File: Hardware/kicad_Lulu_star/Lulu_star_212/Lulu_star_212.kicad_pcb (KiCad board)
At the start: 2 copper layers, 16.7 x 14.9 mm, 6 parts, among them J1 Conn_01x03_Female, Q1 Q_NMOS_GSD, T1 Q_NPN_BEC

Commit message: PCB in progress
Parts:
- LED1: footprint Lulu_footprints:LED_Lulu_side -> Lulu_footprints:Lulu_side_LED
- moved J1 2.90 mm to (123.7, 108.5)
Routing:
- net (no net): vias 0 -> 5
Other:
- board text added: "Lulu V_212"

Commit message: Routing in progress
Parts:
- added J1: Soldering_pad, Lulu_footprints:Lulu_brass_tube_pad, F.Cu at (131.7, 104.8)
- moved R1 0.51 mm to (125.7, 99.8), turned to 180 degrees
- moved Q1 0.25 mm to (128.0, 102.9)
- moved R2 0.15 mm to (130.8, 108.5)
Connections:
- LED1 pad : (no net) -> GND
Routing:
- net Net-(Q1-Pad1): track 0.00 -> 2.27 mm
- net GND: vias 0 -> 4
- net (no net): vias 5 -> 0
- added copper zone on B.Cu, net GND
- added copper zone on F.Cu, net GND
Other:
- board text added: "Lulu"
- board text added: "V-212"
- board text removed: "Lulu V_212"

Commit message: PCB in progress
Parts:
- moved J1 16.0 mm to (139.7, 108.3)
- moved T1 16.0 mm to (140.5, 102.7)
- moved J1 16.0 mm to (147.7, 104.6)
- moved Q1 16.0 mm to (144.0, 102.7)
- moved R2 16.0 mm to (146.8, 108.3)
- moved R1 16.0 mm to (141.7, 99.6)
- moved LED1 16.0 mm to (146.4, 99.9)
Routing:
- net Net-(Q1-Pad2): track 0.00 -> 9.05 mm, vias 0 -> 2
- net Net-(Q1-Pad1): track 2.27 -> 6.60 mm
- net +3V3: track 0.00 -> 1.27 mm
- net Net-(LED1-Pad1): track 0.00 -> 0.65 mm
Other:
- outline, holes or cut-outs redrawn

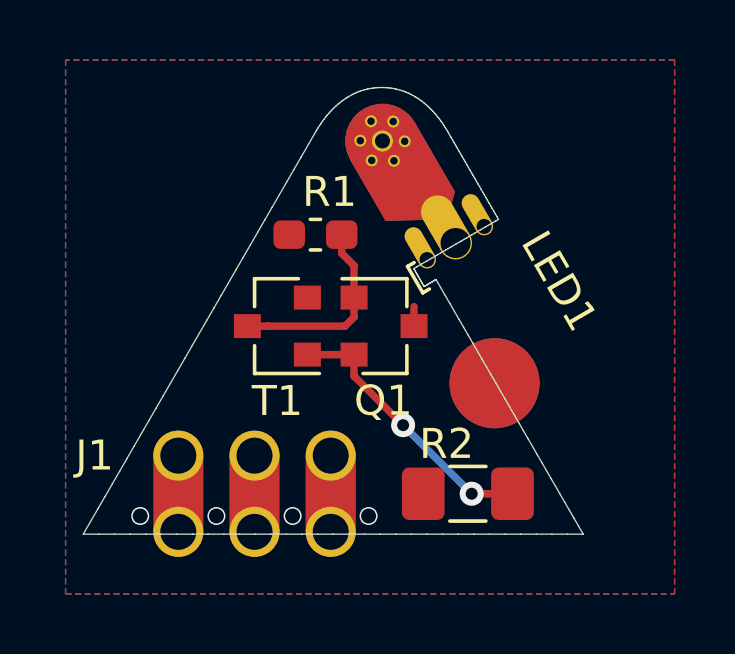
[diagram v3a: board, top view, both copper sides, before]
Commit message: Added PCB pin fonctions top & bottom
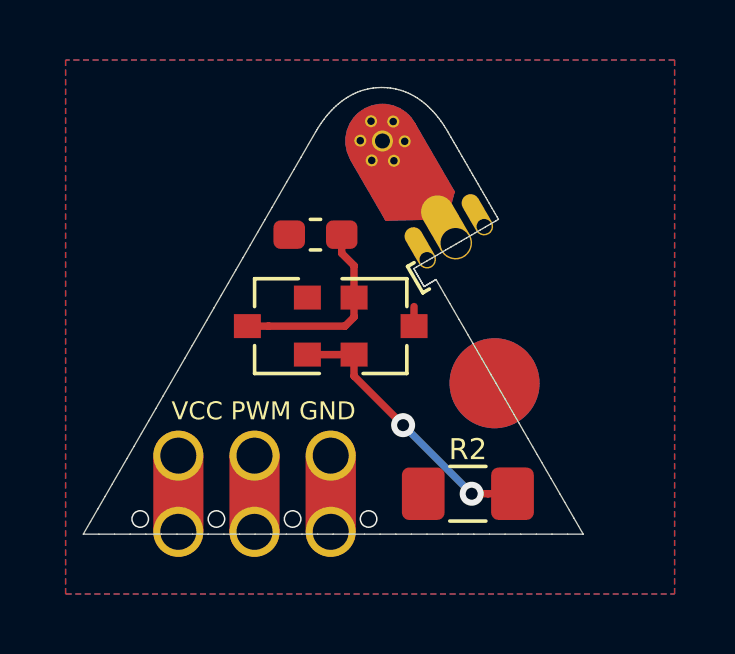
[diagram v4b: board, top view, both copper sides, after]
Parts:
- R1: value 47 K -> 47K
- R2: value 2.7 Ohm -> 2.7-Ohm
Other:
- board text added: "GND PWM VCC"
- board text added: "V.212"
- board text added: "VCC PWM GND"
- board text removed: "V-212"
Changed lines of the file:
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@@
   (general
     (thickness 1)
-    (drawings 290)
+    (drawings 292)
     (tracks 21)
     (zones 0)
@@
     (44 Edge.Cuts user)
     (45 Margin user)
-    (46 B.CrtYd user hide)
-    (47 F.CrtYd user hide)
+    (46 B.CrtYd user)
+    (47 F.CrtYd user)
     (48 B.Fab user)
-    (49 F.Fab user hide)
+    (49 F.Fab user)
   )
   (setup
@@
     (mod_text_size 1 1)
     (mod_text_width 0.15)
-    (pad_size 1.425 1.75)
+    (pad_size 1.675 4.2)
     (pad_drill 0)
     (pad_to_mask_clearance 0)
@@
     (tags "LED Cree XP")
     (attr smd)
-    (fp_text reference LED1 (at 2.35166 2.831161 120.1) (layer F.SilkS)
-      (effects (font (size 1 1) (thickness 0.15)))
-    )
-    (fp_text value LED_PAD (at 2.400901 -2.571716 300.1) (layer F.Fab)
+    (fp_text reference LED1 (at 2.35166 2.831161 120.1) (layer F.SilkS) hide
+      (effects (font (size 1 1) (thickness 0.15)))
+    )
+    (fp_text value LED_PAD (at 2.400901 -2.571716 -59.9) (layer F.Fab) hide
       (effects (font (size 1 1) (thickness 0.15)))
     )
@@
     (pad 3 thru_hole circle (at -1.037581 -4.544671 120.1) (size 0.4 0.4) (drill 0.25) (layers *.Cu)
       (net 2 GND))
-    (pad 3 thru_hole circle (at -0.402581 -4.925671 120.1) (size 0.4 0.4) (drill 0.25) (layers *.Cu)
+    (pad 3 thru_hole circle (at -0.40258 -4.925671 120.1) (size 0.4 0.4) (drill 0.25) (layers *.Cu)
       (net 2 GND))
     (pad 3 thru_hole circle (at -0.402581 -4.163672 120.1) (size 0.7 0.7) (drill 0.5) (layers *.Cu)
@@
     (tags eTextile)
     (zone_connect 0)
-    (fp_text reference J1 (at -5.334 -1.27) (layer F.SilkS)
-      (effects (font (size 1 1) (thickness 0.15)))
-    )
-    (fp_text value Conn_01x03_Female (at 0 3.175) (layer F.Fab)
+    (fp_text reference J1 (at -5.334 -1.27) (layer F.SilkS) hide
+      (effects (font (size 1 1) (thickness 0.15)))
+    )
+    (fp_text value Conn_01x03_Female (at 0 3.175) (layer F.Fab) hide
       (effects (font (size 1 1) (thickness 0.15)))
     )
@@
       (effects (font (size 1 1) (thickness 0.15)))
     )
-    (fp_text value Soldering_pad (at -1.018116 -4.840572 120) (layer F.Fab)
+    (fp_text value Soldering_pad (at -1.018116 -4.840572 120) (layer F.Fab) hide
       (effects (font (size 1 1) (thickness 0.15)))
     )
@@
     (tags SOT-23)
     (attr smd)
-    (fp_text reference T1 (at 0 -2.5 180) (layer F.SilkS)
-      (effects (font (size 1 1) (thickness 0.15)))
-    )
-    (fp_text value Q_NPN_BEC (at 0 2.5 180) (layer F.Fab)
+    (fp_text reference T1 (at 0 -2.5 180) (layer F.SilkS) hide
+      (effects (font (size 1 1) (thickness 0.15)))
+    )
+    (fp_text value Q_NPN_BEC (at 0 2.5 180) (layer F.Fab) hide
       (effects (font (size 1 1) (thickness 0.15)))
     )
@@
       (net 3 "Net-(Q1-Pad1)"))
     (pad 2 smd rect (at -1 0.95 180) (size 0.9 0.8) (layers F.Cu F.Paste F.Mask)
-      (net 2 GND))
+      (net 2 GND) (zone_connect 1))
     (pad 1 smd rect (at -1 -0.95 180) (size 0.9 0.8) (layers F.Cu F.Paste F.Mask)
       (net 1 "Net-(Q1-Pad2)"))
@@
     (tags SOT-23)
     (attr smd)
-    (fp_text reference Q1 (at -0.0254 2.4892) (layer F.SilkS)
-      (effects (font (size 1 1) (thickness 0.15)))
-    )
-    (fp_text value Q_NMOS_GSD (at 0 2.5) (layer F.Fab)
+    (fp_text reference Q1 (at -0.0254 2.4892) (layer F.SilkS) hide
+      (effects (font (size 1 1) (thickness 0.15)))
+    )
+    (fp_text value Q_NMOS_GSD (at 0 2.5) (layer F.Fab) hide
       (effects (font (size 1 1) (thickness 0.15)))
     )
@@
     (tags "resistor handsolder")
     (attr smd)
-    (fp_text reference R1 (at -0.47 1.422 180) (layer F.SilkS)
-      (effects (font (size 1 1) (thickness 0.15)))
-    )
-    (fp_text value "47 K" (at 0 1.43 180) (layer F.Fab)
+    (fp_text reference R1 (at -0.47 1.422 180) (layer F.SilkS) hide
+      (effects (font (size 1 1) (thickness 0.15)))
+    )
+    (fp_text value 47K (at -0.01 1.472 180) (layer F.Fab)
       (effects (font (size 1 1) (thickness 0.15)))
     )
@@
     (tags "resistor handsolder")
     (attr smd)
-    (fp_text reference R2 (at 0.71 1.658 180) (layer F.SilkS)
-      (effects (font (size 1 1) (thickness 0.15)))
-    )
-    (fp_text value "2.7 Ohm" (at -1.016 -2.159 180) (layer F.Fab)
+    (fp_text reference R2 (at 0 1.478 180) (layer F.SilkS)
+      (effects (font (size 0.7 0.7) (thickness 0.12)))
+    )
+    (fp_text value 2.7-Ohm (at -1.016 -2.159 180) (layer F.Fab)
       (effects (font (size 1 1) (thickness 0.15)))
     )
@@
       (rotate (xyz 0 0 0))
     )
+  )
+  (gr_text "GND PWM VCC" (at 140.1 105.4) (layer B.SilkS)
+    (effects (font (size 0.6 0.6) (thickness 0.15)) (justify mirror))
+  )
+  (gr_text "VCC PWM GND" (at 140 105.5) (layer F.SilkS)
+    (effects (font (size 0.6 0.6) (thickness 0.15)))
   )
   (gr_line (start 146.948336 99.624923) (end 146.86014 99.676173) (layer Edge.Cuts) (width 0.01))
@@
   (gr_line (start 145.040124 100.808907) (end 145.050813 100.827693) (layer Edge.Cuts) (width 0.01))
   (gr_line (start 145.89 100.24) (end 145.801806 100.29125) (layer Edge.Cuts) (width 0.01))
-  (gr_text V-212 (at 142.238 102.289 60) (layer B.SilkS)
-    (effects (font (size 1.5 1.5) (thickness 0.3)) (justify mirror))
-  )
-  (gr_text Lulu (at 141.095 99.876 60) (layer B.SilkS)
-    (effects (font (size 1.5 1.5) (thickness 0.3)) (justify mirror))
+  (gr_text V.212 (at 142.7 102.5 60) (layer B.SilkS)
+    (effects (font (size 1 1) (thickness 0.25)) (justify mirror))
+  )
+  (gr_text Lulu (at 141.3 100.7 60) (layer B.SilkS)
+    (effects (font (size 2 2) (thickness 0.4)) (justify mirror))
   )
   (segment (start 141.46 103.62) (end 143.016 103.62) (width 0.25) (layer F.Cu) (net 1))
@@
   (segment (start 143.016 104.337) (end 143.016 103.62) (width 0.25) (layer F.Cu) (net 1))
   (segment (start 144.651 105.972) (end 143.016 104.337) (width 0.25) (layer F.Cu) (net 1))
-  (via (at 143.5 109) (size 0.6) (drill 0.5) (layers F.Cu B.Cu) (net 2))
-  (via (at 140.968 109) (size 0.6) (drill 0.5) (layers F.Cu B.Cu) (net 2))
-  (via (at 138.428 109) (size 0.6) (drill 0.5) (layers F.Cu B.Cu) (net 2))
-  (via (at 135.888 109) (size 0.6) (drill 0.5) (layers F.Cu B.Cu) (net 2))
+  (via (at 143.5 109.1) (size 0.6) (drill 0.5) (layers F.Cu B.Cu) (net 2))
+  (via (at 140.968 109.1) (size 0.6) (drill 0.5) (layers F.Cu B.Cu) (net 2))
+  (via (at 138.428 109.1) (size 0.6) (drill 0.5) (layers F.Cu B.Cu) (net 2))
+  (via (at 135.888 109.1) (size 0.6) (drill 0.5) (layers F.Cu B.Cu) (net 2))
   (segment (start 142.605 99.622) (end 142.605 100.243) (width 0.25) (layer F.Cu) (net 3))
   (segment (start 143.016 100.654) (end 143.016 101.72) (width 0.25) (layer F.Cu) (net 3))

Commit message: Routing done
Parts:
- moved R2 97.0 mm to (74.6, 43.4)
- moved J1 96.5 mm to (67.9, 43.8)
- moved LED1 96.5 mm to (74.6, 35.4)
- moved P1 96.5 mm to (75.9, 40.1), turned to 30 degrees
- moved Q1 96.5 mm to (72.3, 38.2)
- moved T1 96.4 mm to (68.8, 38.2)
- moved R1 95.6 mm to (70.5, 35.8)
- renumbered J1 to P1
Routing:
- net +3V3: track 1.27 -> 21.5 mm
- net /PWM: track 0.00 -> 7.80 mm, vias 0 -> 1
- net Net-(LED1-Pad1): track 0.65 -> 3.43 mm
- net Net-(Q1-Pad1): track 6.60 -> 5.71 mm
- net Net-(Q1-Pad2): track 9.05 -> 8.76 mm, vias 2 -> 0
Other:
- net class Default: clearance 0.2 -> 0.15
- net class POWER added: clearance 0.15, trace_width 0.25, via_dia 0.8, via_drill 0.4
- net class SIG added: clearance 0.15, trace_width 0.15, via_dia 0.8, via_drill 0.4
- rule trace_clearance: 0.2 -> 0.15
- rule trace_min: 0.2 -> 0.15

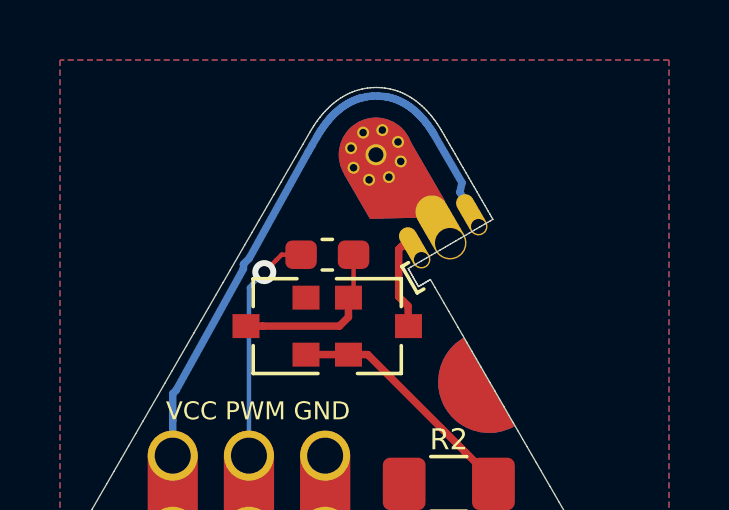
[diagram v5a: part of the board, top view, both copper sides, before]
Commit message: Added Pull down resistor on PWM pin
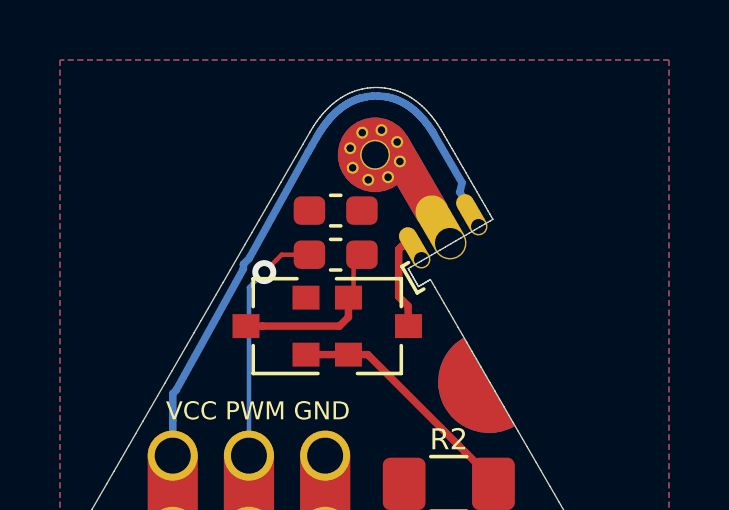
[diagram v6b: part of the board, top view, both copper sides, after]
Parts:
- added R3: 10 K, Resistor_SMD:R_0603_1608Metric_Pad1.05x0.95mm_HandSolder, F.Cu at (70.8, 34.3)
- R1: value 47K -> 47 K
- R2: value 2.7-Ohm -> 2.7 Ohm
- moved R1 0.28 mm to (70.8, 35.8)
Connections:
- LED1 pad : GND -> (no net)
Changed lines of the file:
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@@
     (tracks 99)
     (zones 0)
-    (modules 7)
+    (modules 8)
     (nets 7)
   )
@@
     (mod_text_size 1 1)
     (mod_text_width 0.15)
-    (pad_size 1.425 1.75)
+    (pad_size 1.05 0.95)
     (pad_drill 0)
     (pad_to_mask_clearance 0)
@@
     (fp_line (start -1.778 -0.127) (end -1.524 -0.127) (layer F.SilkS) (width 0.12))
     (fp_arc (start 0 0.6) (end -0.9 0.6) (angle -180) (layer F.Fab) (width 0.1))
-    (pad "" smd custom (at -0.660401 -3.782672 30.1) (size 2.48 2.48) (layers B.Cu B.Mask)
-      (net 2 GND) (zone_connect 2)
+    (pad "" smd custom (at -0.6858 -3.7973 30.1) (size 2.48 2.48) (layers B.Cu B.SilkS)
+      (zone_connect 2)
       (options (clearance outline) (anchor circle))
       (primitives
         (gr_poly (pts
-           (xy -1.2446 0.023472) (xy 1.2192 0.023472) (xy 1.2192 1.750672) (xy -1.2446 1.750672)) (width 0))
-        (gr_poly (pts
-           (xy 1.2192 2.512672) (xy 1.2192 1.750672) (xy -1.2446 1.750672) (xy 0.1524 2.512672)) (width 0))
+           (xy 1.244601 2.652372) (xy 1.244601 -0.014628) (xy 0.127001 -0.014628) (xy 0.127001 2.652372)) (width 0))
       ))
-    (pad "" smd custom (at -0.660401 -3.782672 30.1) (size 2.48 2.48) (layers F.Cu F.Mask)
-      (net 2 GND) (zone_connect 2)
+    (pad "" smd custom (at -0.685801 -3.795372 30.1) (size 2.48 2.48) (layers F.Cu F.Mask)
+      (zone_connect 2)
       (options (clearance outline) (anchor circle))
       (primitives
         (gr_poly (pts
-           (xy -1.2446 0.023472) (xy 1.2192 0.023472) (xy 1.2192 1.750672) (xy -1.2446 1.750672)) (width 0))
-        (gr_poly (pts
-           (xy 1.2192 2.512672) (xy 1.2192 1.750672) (xy -1.2446 1.750672) (xy 0.1524 2.512672)) (width 0))
+           (xy 1.244601 2.652372) (xy 1.244601 -0.014628) (xy 0.127001 -0.014628) (xy 0.127001 2.652372)) (width 0))
       ))
-    (pad 3 thru_hole circle (at -1.268427 -4.388906 75.1) (size 0.4 0.4) (drill 0.25) (layers *.Cu)
-      (net 2 GND))
-    (pad 3 thru_hole circle (at -0.056093 -3.176572 75.1) (size 0.4 0.4) (drill 0.25) (layers *.Cu)
-      (net 2 GND))
-    (pad 3 thru_hole circle (at -1.276044 -3.17521 75.1) (size 0.4 0.4) (drill 0.25) (layers *.Cu)
-      (net 2 GND))
-    (pad 3 thru_hole circle (at -0.06371 -4.387544 75.1) (size 0.4 0.4) (drill 0.25) (layers *.Cu)
-      (net 2 GND))
-    (pad 3 thru_hole circle (at -0.6604 -4.6355 30.1) (size 0.4 0.4) (drill 0.25) (layers *.Cu)
-      (net 2 GND))
-    (pad 3 thru_hole circle (at -0.6604 -2.921 30.1) (size 0.4 0.4) (drill 0.25) (layers *.Cu)
-      (net 2 GND))
-    (pad 3 thru_hole circle (at 0.1905 -3.782672 30.1) (size 0.4 0.4) (drill 0.25) (layers *.Cu)
+    (pad 3 thru_hole circle (at -1.293827 -4.401606 75.1) (size 0.4 0.4) (drill 0.25) (layers *.Cu)
+      (net 2 GND))
+    (pad 3 thru_hole circle (at -0.081493 -3.189272 75.1) (size 0.4 0.4) (drill 0.25) (layers *.Cu)
+      (net 2 GND))
+    (pad 3 thru_hole circle (at -1.301444 -3.18791 75.1) (size 0.4 0.4) (drill 0.25) (layers *.Cu)
+      (net 2 GND))
+    (pad 3 thru_hole circle (at -0.08911 -4.400244 75.1) (size 0.4 0.4) (drill 0.25) (layers *.Cu)
+      (net 2 GND))
+    (pad 3 thru_hole circle (at -0.6858 -4.6482 30.1) (size 0.4 0.4) (drill 0.25) (layers *.Cu)
+      (net 2 GND))
+    (pad 3 thru_hole circle (at -0.6858 -2.9337 30.1) (size 0.4 0.4) (drill 0.25) (layers *.Cu)
+      (net 2 GND))
+    (pad 3 thru_hole circle (at 0.1651 -3.795372 30.1) (size 0.4 0.4) (drill 0.25) (layers *.Cu)
       (net 2 GND))
     (pad 3 thru_hole oval (at 0 0 30.1) (size 1.1 2.3) (drill 1 (offset 0 -0.6)) (layers *.Cu *.Mask)
@@
     (pad 2 thru_hole oval (at 1.1 0 30.1) (size 0.6 1.5) (drill 0.5 (offset 0 -0.45)) (layers *.Cu *.Mask)
       (net 6 +3V3) (zone_connect 0))
-    (pad 3 thru_hole circle (at -0.660401 -3.782672 120.1) (size 0.7 0.7) (drill 0.5) (layers *.Cu)
-      (net 2 GND))
-    (pad 3 thru_hole circle (at -1.524 -3.782672 30.1) (size 0.4 0.4) (drill 0.25) (layers *.Cu)
+    (pad 3 thru_hole circle (at -0.685801 -3.795372 120.1) (size 1 1) (drill 0.9) (layers *.Cu)
+      (net 2 GND))
+    (pad 3 thru_hole circle (at -1.5494 -3.795372 30.1) (size 0.4 0.4) (drill 0.25) (layers *.Cu)
       (net 2 GND))
     (model /home/chevrette/Bureau/Lulu/Hardware/kicad_Lulu_star/Lulu_star_212/packages3D/Lulu_LED_tube.wrl
+      (at (xyz 0 0 0))
+      (scale (xyz 1 1 1))
+      (rotate (xyz 0 0 0))
+    )
+  )
+  (module Resistor_SMD:R_0603_1608Metric_Pad1.05x0.95mm_HandSolder (layer F.Cu)
+    (at 70.83 34.32)
+    (descr "Resistor SMD 0603 (1608 Metric), square (rectangular) end terminal, IPC_7351 nominal with elongated pad for handsoldering. (Body size source: http://www.tortai-tech.com/upload/download/2011102023233369053.pdf), generated with kicad-footprint-generator")
+    (tags "resistor handsolder")
+    (attr smd)
+    (fp_text reference R3 (at 0 -1.43) (layer F.SilkS) hide
+      (effects (font (size 1 1) (thickness 0.15)))
+    )
+    (fp_text value "10 K" (at 0 1.43) (layer F.Fab)
+      (effects (font (size 1 1) (thickness 0.15)))
+    )
+    (fp_line (start -0.8 0.4) (end -0.8 -0.4) (layer F.Fab) (width 0.1))
+    (fp_line (start -0.8 -0.4) (end 0.8 -0.4) (layer F.Fab) (width 0.1))
+    (fp_line (start 0.8 -0.4) (end 0.8 0.4) (layer F.Fab) (width 0.1))
+    (fp_line (start 0.8 0.4) (end -0.8 0.4) (layer F.Fab) (width 0.1))
+    (fp_line (start -0.171267 -0.51) (end 0.171267 -0.51) (layer F.SilkS) (width 0.12))
+    (fp_line (start -0.171267 0.51) (end 0.171267 0.51) (layer F.SilkS) (width 0.12))
+    (fp_line (start -1.65 0.73) (end -1.65 -0.73) (layer F.CrtYd) (width 0.05))
+    (fp_line (start -1.65 -0.73) (end 1.65 -0.73) (layer F.CrtYd) (width 0.05))
+    (fp_line (start 1.65 -0.73) (end 1.65 0.73) (layer F.CrtYd) (width 0.05))
+    (fp_line (start 1.65 0.73) (end -1.65 0.73) (layer F.CrtYd) (width 0.05))
+    (fp_text user %R (at 0 0) (layer F.Fab)
+      (effects (font (size 0.4 0.4) (thickness 0.06)))
+    )
+    (pad 1 smd roundrect (at -0.875 0) (size 1.05 0.95) (layers F.Cu F.Paste F.Mask) (roundrect_rratio 0.25)
+      (net 4 /PWM))
+    (pad 2 smd roundrect (at 0.875 0) (size 1.05 0.95) (layers F.Cu F.Paste F.Mask) (roundrect_rratio 0.25)
+      (net 2 GND) (zone_connect 1))
+    (model ${KISYS3DMOD}/Resistor_SMD.3dshapes/R_0603_1608Metric.wrl
       (at (xyz 0 0 0))
       (scale (xyz 1 1 1))
@@
   )
   (module Resistor_SMD:R_0603_1608Metric_Pad1.05x0.95mm_HandSolder (layer F.Cu)
-    (at 70.55 35.79 180)
+    (at 70.83 35.79 180)
     (descr "Resistor SMD 0603 (1608 Metric), square (rectangular) end terminal, IPC_7351 nominal with elongated pad for handsoldering. (Body size source: http://www.tortai-tech.com/upload/download/2011102023233369053.pdf), generated with kicad-footprint-generator")
     (tags "resistor handsolder")
@@
       (effects (font (size 1 1) (thickness 0.15)))
     )
-    (fp_text value 47K (at -0.01 1.472 180) (layer F.Fab)
+    (fp_text value "47 K" (at -0.01 1.472 180) (layer F.Fab)
       (effects (font (size 1 1) (thickness 0.15)))
     )
@@
       (effects (font (size 0.7 0.7) (thickness 0.12)))
     )
-    (fp_text value 2.7-Ohm (at -1.016 -2.159 180) (layer F.Fab)
-      (effects (font (size 1 1) (thickness 0.15)))
-    )
+    (fp_text value "2.7 Ohm" (at -1.016 -2.159 180) (layer F.Fab)
+      (effects (font (size 1 1) (thickness 0.15)))
+    )
